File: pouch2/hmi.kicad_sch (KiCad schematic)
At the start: 20 parts, among them J1 Conn_01x14_Male, J2 Conn_01x14_Male, J3 Conn_01x14_Male, J4 Conn_01x14_Male, J5 Conn_01x14_Male, J6 Conn_01x14_Male, J7 Conn_01x14_Male, J8 Conn_01x14_Male, SW2 SW_DIP_x08

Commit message: added pi zero header
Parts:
- J1, J2, J3, J4, J5, J6, J7, J8: footprint (none) -> Connector_PinHeader_2.54mm:PinHeader_1x14_P2.54mm_Horizontal
- R36, R37, R38, R39, R40, R41, R42, R43: footprint (none) -> Resistor_SMD:R_0815_2038Metric
- SW2: footprint (none) -> Package_DIP:DIP-16_W7.62mm
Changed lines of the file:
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@@
 			)
 		)
-		(property "Footprint" ""
+		(property "Footprint" "Resistor_SMD:R_0815_2038Metric"
 			(at 59.69 112.268 90)
 			(effects
@@
 			)
 		)
-		(property "Footprint" ""
+		(property "Footprint" "Resistor_SMD:R_0815_2038Metric"
 			(at 87.63 24.638 90)
 			(effects
@@
 			)
 		)
-		(property "Footprint" ""
+		(property "Footprint" "Resistor_SMD:R_0815_2038Metric"
 			(at 87.63 55.118 90)
 			(effects
@@
 			)
 		)
-		(property "Footprint" ""
+		(property "Footprint" "Connector_PinHeader_2.54mm:PinHeader_1x14_P2.54mm_Horizontal"
 			(at 219.71 107.95 0)
 			(effects
@@
 			)
 		)
-		(property "Footprint" ""
+		(property "Footprint" "Connector_PinHeader_2.54mm:PinHeader_1x14_P2.54mm_Horizontal"
 			(at 172.72 107.95 0)
 			(effects
@@
 			)
 		)
-		(property "Footprint" ""
+		(property "Footprint" "Resistor_SMD:R_0815_2038Metric"
 			(at 87.63 34.798 90)
 			(effects
@@
 			)
 		)
-		(property "Footprint" ""
+		(property "Footprint" "Resistor_SMD:R_0815_2038Metric"
 			(at 87.63 44.958 90)
 			(effects
@@
 			)
 		)
-		(property "Footprint" ""
+		(property "Footprint" "Connector_PinHeader_2.54mm:PinHeader_1x14_P2.54mm_Horizontal"
 			(at 252.73 107.95 0)
 			(effects
@@
 			)
 		)
-		(property "Footprint" ""
+		(property "Footprint" "Connector_PinHeader_2.54mm:PinHeader_1x14_P2.54mm_Horizontal"
 			(at 157.48 107.95 0)
 			(effects
@@
 			)
 		)
-		(property "Footprint" ""
+		(property "Footprint" "Resistor_SMD:R_0815_2038Metric"
 			(at 59.69 137.668 90)
 			(effects
@@
 			)
 		)
-		(property "Footprint" ""
+		(property "Footprint" "Package_DIP:DIP-16_W7.62mm"
 			(at 45.72 55.88 0)
 			(effects
@@
 			)
 		)
-		(property "Footprint" ""
+		(property "Footprint" "Resistor_SMD:R_0815_2038Metric"
 			(at 94.742 57.15 90)
 			(effects
@@
 			)
 		)
-		(property "Footprint" ""
+		(property "Footprint" "Connector_PinHeader_2.54mm:PinHeader_1x14_P2.54mm_Horizontal"
 			(at 267.97 107.95 0)
 			(effects
@@
 			)
 		)
-		(property "Footprint" ""
+		(property "Footprint" "Resistor_SMD:R_0815_2038Metric"
 			(at 59.69 124.968 90)
 			(effects
@@
 			)
 		)
-		(property "Footprint" ""
+		(property "Footprint" "Connector_PinHeader_2.54mm:PinHeader_1x14_P2.54mm_Horizontal"
 			(at 190.5 107.95 0)
 			(effects
@@
 			)
 		)
-		(property "Footprint" ""
+		(property "Footprint" "Connector_PinHeader_2.54mm:PinHeader_1x14_P2.54mm_Horizontal"
 			(at 234.95 107.95 0)
 			(effects
@@
 			)
 		)
-		(property "Footprint" ""
+		(property "Footprint" "Connector_PinHeader_2.54mm:PinHeader_1x14_P2.54mm_Horizontal"
 			(at 205.74 107.95 0)
 			(effects

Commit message: started PCB design
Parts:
- D701: renamed from D1; footprint (none) -> LED_THT:LED_D5.0mm
- D702: renamed from D2; footprint (none) -> LED_THT:LED_D5.0mm
- D703: renamed from D3; footprint (none) -> LED_THT:LED_D5.0mm
- J701: renamed from J1; footprint Connector_PinHeader_2.54mm:PinHeader_1x14_P2.54mm_Horizontal -> Connector_PinHeader_2.54mm:PinHeader_1x14_P2.54mm_Vertical
- J702: renamed from J2; footprint Connector_PinHeader_2.54mm:PinHeader_1x14_P2.54mm_Horizontal -> Connector_PinHeader_2.54mm:PinHeader_1x14_P2.54mm_Vertical
- J703: renamed from J3; footprint Connector_PinHeader_2.54mm:PinHeader_1x14_P2.54mm_Horizontal -> Connector_PinHeader_2.54mm:PinHeader_1x14_P2.54mm_Vertical
- J704: renamed from J4; footprint Connector_PinHeader_2.54mm:PinHeader_1x14_P2.54mm_Horizontal -> Connector_PinHeader_2.54mm:PinHeader_1x14_P2.54mm_Vertical
- J705: renamed from J5; footprint Connector_PinHeader_2.54mm:PinHeader_1x14_P2.54mm_Horizontal -> Connector_PinHeader_2.54mm:PinHeader_1x14_P2.54mm_Vertical
- J706: renamed from J6; footprint Connector_PinHeader_2.54mm:PinHeader_1x14_P2.54mm_Horizontal -> Connector_PinHeader_2.54mm:PinHeader_1x14_P2.54mm_Vertical
- J707: renamed from J7; footprint Connector_PinHeader_2.54mm:PinHeader_1x14_P2.54mm_Horizontal -> Connector_PinHeader_2.54mm:PinHeader_1x14_P2.54mm_Vertical
- J708: renamed from J8; footprint Connector_PinHeader_2.54mm:PinHeader_1x14_P2.54mm_Horizontal -> Connector_PinHeader_2.54mm:PinHeader_1x14_P2.54mm_Vertical
- R701: renamed from R36; footprint Resistor_SMD:R_0815_2038Metric -> Resistor_SMD:R_0805_2012Metric
- R702: renamed from R37; footprint Resistor_SMD:R_0815_2038Metric -> Resistor_SMD:R_0805_2012Metric
- R703: renamed from R38; footprint Resistor_SMD:R_0815_2038Metric -> Resistor_SMD:R_0805_2012Metric
- R704: renamed from R43; footprint Resistor_SMD:R_0815_2038Metric -> Resistor_SMD:R_0805_2012Metric
- R705: renamed from R42; footprint Resistor_SMD:R_0815_2038Metric -> Resistor_SMD:R_0805_2012Metric
- R706: renamed from R41; footprint Resistor_SMD:R_0815_2038Metric -> Resistor_SMD:R_0805_2012Metric
- R707: renamed from R40; footprint Resistor_SMD:R_0815_2038Metric -> Resistor_SMD:R_0805_2012Metric
- R708: renamed from R39; footprint Resistor_SMD:R_0815_2038Metric -> Resistor_SMD:R_0805_2012Metric
- renumbered SW2 to SW701

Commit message: PCB and footprint arrangements
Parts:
- SW701: footprint Package_DIP:DIP-16_W7.62mm -> Button_Switch_THT:SW_DIP_SPSTx08_Slide_9.78x22.5mm_W7.62mm_P2.54mm
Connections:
- net GND: now also J708.14 (Pin_14)
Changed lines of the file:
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@@
-	(wire
-		(pts
-			(xy 271.78 128.27) (xy 271.78 124.46)
-		)
-		(stroke
-			(width 0)
-			(type default)
-		)
-	)
 	(wire
 		(pts
@@
 	(wire
 		(pts
+			(xy 273.05 125.73) (xy 273.05 128.27)
+		)
+		(stroke
+			(width 0)
+			(type default)
+		)
+	)
+	(wire
+		(pts
 			(xy 224.79 92.71) (xy 224.79 86.36)
 		)
@@
 	(wire
 		(pts
-			(xy 257.81 128.27) (xy 271.78 128.27)
+			(xy 257.81 128.27) (xy 273.05 128.27)
 		)
 		(stroke
@@
 			)
 		)
-		(property "Footprint" "Package_DIP:DIP-16_W7.62mm"
+		(property "Footprint" "Button_Switch_THT:SW_DIP_SPSTx08_Slide_9.78x22.5mm_W7.62mm_P2.54mm"
 			(at 45.72 55.88 0)
 			(effects

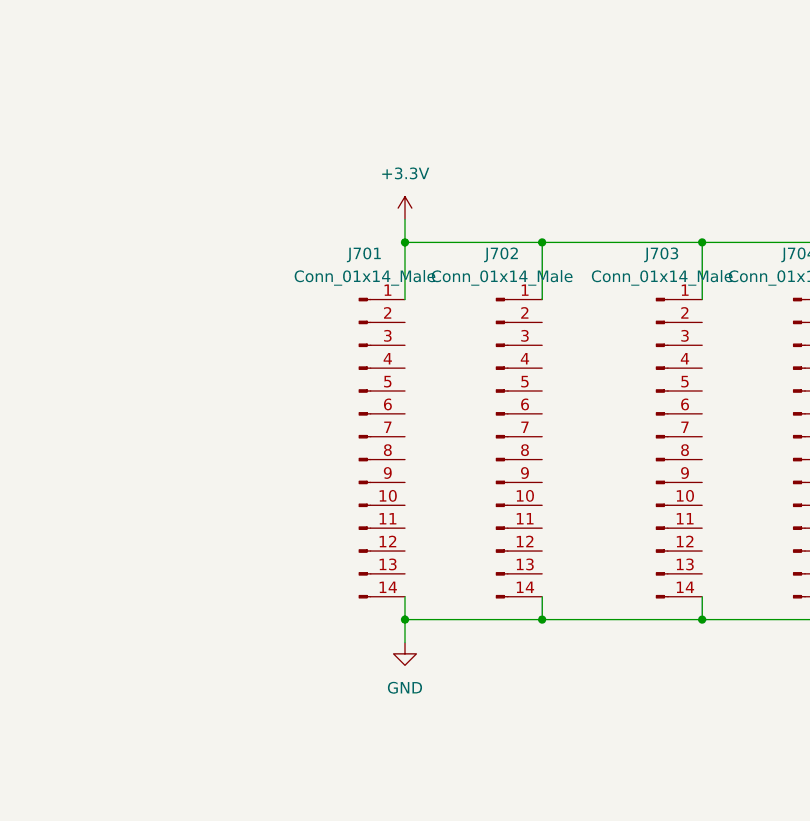
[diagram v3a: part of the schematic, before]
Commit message: updated backside of PCB
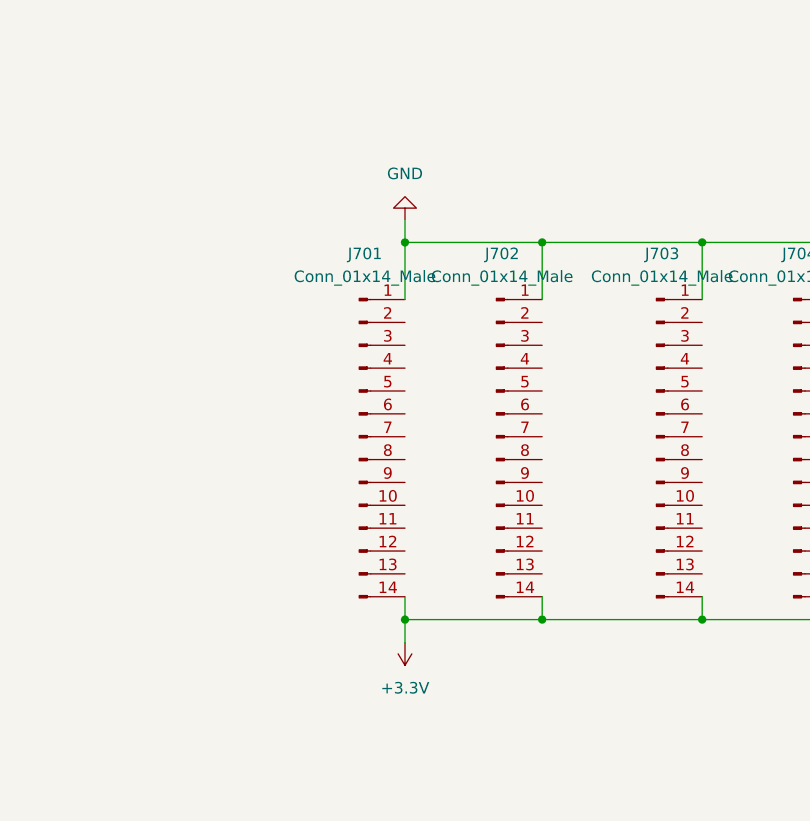
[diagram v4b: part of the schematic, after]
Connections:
- net +3.3V: now also J701.14 (Pin_14), J702.14 (Pin_14), J703.14 (Pin_14), J704.14 (Pin_14), J705.14 (Pin_14), J706.14 (Pin_14), J707.14 (Pin_14), J708.14 (Pin_14); no longer J701.1 (Pin_1), J702.1 (Pin_1), J703.1 (Pin_1), J704.1 (Pin_1), J705.1 (Pin_1), J706.1 (Pin_1), J707.1 (Pin_1), J708.1 (Pin_1)
- net GND: now also J701.1 (Pin_1), J702.1 (Pin_1), J703.1 (Pin_1), J704.1 (Pin_1), J705.1 (Pin_1), J706.1 (Pin_1), J707.1 (Pin_1), J708.1 (Pin_1); no longer J701.14 (Pin_14), J702.14 (Pin_14), J703.14 (Pin_14), J704.14 (Pin_14), J705.14 (Pin_14), J706.14 (Pin_14), J707.14 (Pin_14), J708.14 (Pin_14)
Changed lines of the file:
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@@
+	)
+	(symbol
+		(lib_id "power:GND")
+		(at 162.56 83.82 180)
+		(unit 1)
+		(exclude_from_sim no)
+		(in_bom yes)
+		(on_board yes)
+		(dnp no)
+		(fields_autoplaced yes)
+		(property "Reference" "#PWR0705"
+			(at 162.56 77.47 0)
+			(effects
+				(font
+					(size 1.27 1.27)
+				)
+				(hide yes)
+			)
+		)
+		(property "Value" "GND"
+			(at 162.56 78.74 0)
+			(effects
+				(font
+					(size 1.27 1.27)
+				)
+			)
+		)
+		(property "Footprint" ""
+			(at 162.56 83.82 0)
+			(effects
+				(font
+					(size 1.27 1.27)
+				)
+				(hide yes)
+			)
+		)
+		(property "Datasheet" ""
+			(at 162.56 83.82 0)
+			(effects
+				(font
+					(size 1.27 1.27)
+				)
+				(hide yes)
+			)
+		)
+		(property "Description" "Power symbol creates a global label with name \"GND\" , ground"
+			(at 162.56 83.82 0)
+			(effects
+				(font
+					(size 1.27 1.27)
+				)
+				(hide yes)
+			)
+		)
+		(pin "1"
+		)
+		(instances
+			(project "pouch2"
+				(path "/278cfa6b-9496-4a22-b425-8abdb96793ef/dcbcf723-f7ed-4082-a41f-9f6fc76b941a"
+					(reference "#PWR0705")
+					(unit 1)
+				)
+			)
+		)
+	)
+	(symbol
+		(lib_id "power:+3.3V")
+		(at 162.56 130.81 180)
+		(unit 1)
+		(exclude_from_sim no)
+		(in_bom yes)
+		(on_board yes)
+		(dnp no)
+		(fields_autoplaced yes)
+		(property "Reference" "#PWR0704"
+			(at 162.56 127 0)
+			(effects
+				(font
+					(size 1.27 1.27)
+				)
+				(hide yes)
+			)
+		)
+		(property "Value" "+3.3V"
+			(at 162.56 135.89 0)
+			(effects
+				(font
+					(size 1.27 1.27)
+				)
+			)
+		)
+		(property "Footprint" ""
+			(at 162.56 130.81 0)
+			(effects
+				(font
+					(size 1.27 1.27)
+				)
+				(hide yes)
+			)
+		)
+		(property "Datasheet" ""
+			(at 162.56 130.81 0)
+			(effects
+				(font
+					(size 1.27 1.27)
+				)
+				(hide yes)
+			)
+		)
+		(property "Description" "Power symbol creates a global label with name \"+3.3V\""
+			(at 162.56 130.81 0)
+			(effects
+				(font
+					(size 1.27 1.27)
+				)
+				(hide yes)
+			)
+		)
+		(pin "1"
+		)
+		(instances
+			(project "pouch2"
+				(path "/278cfa6b-9496-4a22-b425-8abdb96793ef/dcbcf723-f7ed-4082-a41f-9f6fc76b941a"
+					(reference "#PWR0704")
+					(unit 1)
+				)
+			)
+		)
 	)
 	(symbol
@@
 	)
 	(symbol
-		(lib_id "power:GND")
-		(at 162.56 130.81 0)
-		(unit 1)
-		(exclude_from_sim no)
-		(in_bom yes)
-		(on_board yes)
-		(dnp no)
-		(fields_autoplaced yes)
-		(property "Reference" "#PWR0705"
-			(at 162.56 137.16 0)
-			(effects
-				(font
-					(size 1.27 1.27)
-				)
-				(hide yes)
-			)
-		)
-		(property "Value" "GND"
-			(at 162.56 135.89 0)
-			(effects
-				(font
-					(size 1.27 1.27)
-				)
-			)
-		)
-		(property "Footprint" ""
-			(at 162.56 130.81 0)
-			(effects
-				(font
-					(size 1.27 1.27)
-				)
-				(hide yes)
-			)
-		)
-		(property "Datasheet" ""
-			(at 162.56 130.81 0)
-			(effects
-				(font
-					(size 1.27 1.27)
-				)
-				(hide yes)
-			)
-		)
-		(property "Description" "Power symbol creates a global label with name \"GND\" , ground"
-			(at 162.56 130.81 0)
-			(effects
-				(font
-					(size 1.27 1.27)
-				)
-				(hide yes)
-			)
-		)
-		(pin "1"
-		)
-		(instances
-			(project ""
-				(path "/278cfa6b-9496-4a22-b425-8abdb96793ef/dcbcf723-f7ed-4082-a41f-9f6fc76b941a"
-					(reference "#PWR0705")
-					(unit 1)
-				)
-			)
-		)
-	)
-	(symbol
 		(lib_id "Device:LED")
 		(at 71.12 135.89 180)
@@
 					(unit 1)
 				)
-			)
-		)
-	)
-	(symbol
-		(lib_id "power:+3.3V")
-		(at 162.56 83.82 0)
-		(unit 1)
-		(exclude_from_sim no)
-		(in_bom yes)
-		(on_board yes)
-		(dnp no)
-		(fields_autoplaced yes)
-		(property "Reference" "#PWR0704"
-			(at 162.56 87.63 0)
-			(effects
-				(font
-					(size 1.27 1.27)
-				)
-				(hide yes)
-			)
-		)
-		(property "Value" "+3.3V"
-			(at 162.56 78.74 0)
-			(effects
-				(font
-					(size 1.27 1.27)
-				)
-			)
-		)
-		(property "Footprint" ""
-			(at 162.56 83.82 0)
-			(effects
-				(font
-					(size 1.27 1.27)
-				)
-				(hide yes)
-			)
-		)
-		(property "Datasheet" ""
-			(at 162.56 83.82 0)
-			(effects
-				(font
-					(size 1.27 1.27)
-				)
-				(hide yes)
-			)
-		)
-		(property "Description" "Power symbol creates a global label with name \"+3.3V\""
-			(at 162.56 83.82 0)
-			(effects
-				(font
-					(size 1.27 1.27)
-				)
-				(hide yes)
-			)
-		)
-		(pin "1"
-		)
-		(instances
-			(project ""
-				(path "/278cfa6b-9496-4a22-b425-8abdb96793ef/dcbcf723-f7ed-4082-a41f-9f6fc76b941a"
-					(reference "#PWR0704")
-					(unit 1)
-				)

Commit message: started routing
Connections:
- net HMI_S34: now reaches SW701.10
- net HMI_S24: now reaches SW701.11
- net HMI_S14: now reaches SW701.12
- net HMI_S13: now reaches SW701.5
- net HMI_S23: now reaches SW701.6
- net HMI_S33: now reaches SW701.7
- net HMI_S43: now reaches SW701.8
- net HMI_S44: now reaches SW701.9
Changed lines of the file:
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@@
+	(wire
+		(pts
+			(xy 53.34 58.42) (xy 64.77 58.42)
+		)
+		(stroke
+			(width 0)
+			(type default)
+		)
+	)
 	(wire
 		(pts
@@
 	(wire
 		(pts
+			(xy 27.94 55.88) (xy 38.1 55.88)
+		)
+		(stroke
+			(width 0)
+			(type default)
+		)
+	)
+	(wire
+		(pts
 			(xy 91.44 53.34) (xy 96.52 53.34)
 		)
@@
 	(wire
 		(pts
+			(xy 27.94 60.96) (xy 38.1 60.96)
+		)
+		(stroke
+			(width 0)
+			(type default)
+		)
+	)
+	(wire
+		(pts
 			(xy 100.33 22.86) (xy 96.52 22.86)
 		)
@@
 	(wire
 		(pts
+			(xy 53.34 63.5) (xy 64.77 63.5)
+		)
+		(stroke
+			(width 0)
+			(type default)
+		)
+	)
+	(wire
+		(pts
+			(xy 27.94 63.5) (xy 38.1 63.5)
+		)
+		(stroke
+			(width 0)
+			(type default)
+		)
+	)
+	(wire
+		(pts
+			(xy 53.34 60.96) (xy 64.77 60.96)
+		)
+		(stroke
+			(width 0)
+			(type default)
+		)
+	)
+	(wire
+		(pts
 			(xy 46.99 110.49) (xy 55.88 110.49)
 		)
@@
 	(wire
 		(pts
+			(xy 53.34 55.88) (xy 64.77 55.88)
+		)
+		(stroke
+			(width 0)
+			(type default)
+		)
+	)
+	(wire
+		(pts
 			(xy 53.34 45.72) (xy 77.47 45.72)
 		)
@@
 	(wire
 		(pts
+			(xy 27.94 58.42) (xy 38.1 58.42)
+		)
+		(stroke
+			(width 0)
+			(type default)
+		)
+	)
+	(wire
+		(pts
 			(xy 74.93 135.89) (xy 81.28 135.89)
 		)
@@
 		)
 	)
+	(global_label "HMI_S24"
+		(shape input)
+		(at 64.77 58.42 0)
+		(fields_autoplaced yes)
+		(effects
+			(font
+				(size 1.27 1.27)
+			)
+			(justify left)
+		)
+		(property "Intersheetrefs" "${INTERSHEET_REFS}"
+			(at 75.738 58.42 0)
+			(effects
+				(font
+					(size 1.27 1.27)
+				)
+				(justify left)
+				(hide yes)
+			)
+		)
+	)
+	(global_label "HMI_S44"
+		(shape input)
+		(at 64.77 63.5 0)
+		(fields_autoplaced yes)
+		(effects
+			(font
+				(size 1.27 1.27)
+			)
+			(justify left)
+		)
+		(property "Intersheetrefs" "${INTERSHEET_REFS}"
+			(at 75.738 63.5 0)
+			(effects
+				(font
+					(size 1.27 1.27)
+				)
+				(justify left)
+				(hide yes)
+			)
+		)
+	)
+	(global_label "HMI_S33"
+		(shape input)
+		(at 27.94 60.96 180)
+		(fields_autoplaced yes)
+		(effects
+			(font
+				(size 1.27 1.27)
+			)
+			(justify right)
+		)
+		(property "Intersheetrefs" "${INTERSHEET_REFS}"
+			(at 16.972 60.96 0)
+			(effects
+				(font
+					(size 1.27 1.27)
+				)
+				(justify right)
+				(hide yes)
+			)
+		)
+	)
+	(global_label "HMI_S34"
+		(shape input)
+		(at 64.77 60.96 0)
+		(fields_autoplaced yes)
+		(effects
+			(font
+				(size 1.27 1.27)
+			)
+			(justify left)
+		)
+		(property "Intersheetrefs" "${INTERSHEET_REFS}"
+			(at 75.738 60.96 0)
+			(effects
+				(font
+					(size 1.27 1.27)
+				)
+				(justify left)
+				(hide yes)
+			)
+		)
+	)
+	(global_label "HMI_S13"
+		(shape input)
+		(at 27.94 55.88 180)
+		(fields_autoplaced yes)
+		(effects
+			(font
+				(size 1.27 1.27)
+			)
+			(justify right)
+		)
+		(property "Intersheetrefs" "${INTERSHEET_REFS}"
+			(at 16.972 55.88 0)
+			(effects
+				(font
+					(size 1.27 1.27)
+				)
+				(justify right)
+				(hide yes)
+			)
+		)
+	)
+	(global_label "HMI_S43"
+		(shape input)
+		(at 27.94 63.5 180)
+		(fields_autoplaced yes)
+		(effects
+			(font
+				(size 1.27 1.27)
+			)
+			(justify right)
+		)
+		(property "Intersheetrefs" "${INTERSHEET_REFS}"
+			(at 16.972 63.5 0)
+			(effects
+				(font
+					(size 1.27 1.27)
+				)
+				(justify right)
+				(hide yes)
+			)
+		)
+	)
+	(global_label "HMI_S23"
+		(shape input)
+		(at 27.94 58.42 180)
+		(fields_autoplaced yes)
+		(effects
+			(font
+				(size 1.27 1.27)
+			)
+			(justify right)
+		)
+		(property "Intersheetrefs" "${INTERSHEET_REFS}"
+			(at 16.972 58.42 0)
+			(effects
+				(font
+					(size 1.27 1.27)
+				)
+				(justify right)
+				(hide yes)
+			)
+		)
+	)
+	(global_label "HMI_S14"
+		(shape input)
+		(at 64.77 55.88 0)
+		(fields_autoplaced yes)
+		(effects
+			(font
+				(size 1.27 1.27)
+			)
+			(justify left)
+		)
+		(property "Intersheetrefs" "${INTERSHEET_REFS}"
+			(at 75.738 55.88 0)
+			(effects
+				(font
+					(size 1.27 1.27)
+				)
+				(justify left)
+				(hide yes)
+			)
+		)
+	)
